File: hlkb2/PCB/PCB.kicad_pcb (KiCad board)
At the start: 2 copper layers, 228 x 76 mm, 101 parts, among them K1 KEYSW, K10 KEYSW, K11 KEYSW, K12 KEYSW, K13 KEYSW, K14 KEYSW, K15 KEYSW, K16 KEYSW, K17 KEYSW, K18 KEYSW, K19 KEYSW, K2 KEYSW, K20 KEYSW, K21 KEYSW, K22 KEYSW, K23 KEYSW, K24 KEYSW, K25 KEYSW, K26 KEYSW, K27 KEYSW, K28 KEYSW, K29 KEYSW, K3 KEYSW, K30 KEYSW, K31 KEYSW, K32 KEYSW, K33 KEYSW, K34 KEYSW, K35 KEYSW, K36 KEYSW, K37 KEYSW, K38 KEYSW, K39 KEYSW, K4 KEYSW, K40 KEYSW, K41 KEYSW, K42 KEYSW, K43 KEYSW, K44 KEYSW, K45 KEYSW, K46 KEYSW, K47 KEYSW, K48 KEYSW, K5 KEYSW, K6 KEYSW, K7 KEYSW, K8 KEYSW, K9 KEYSW

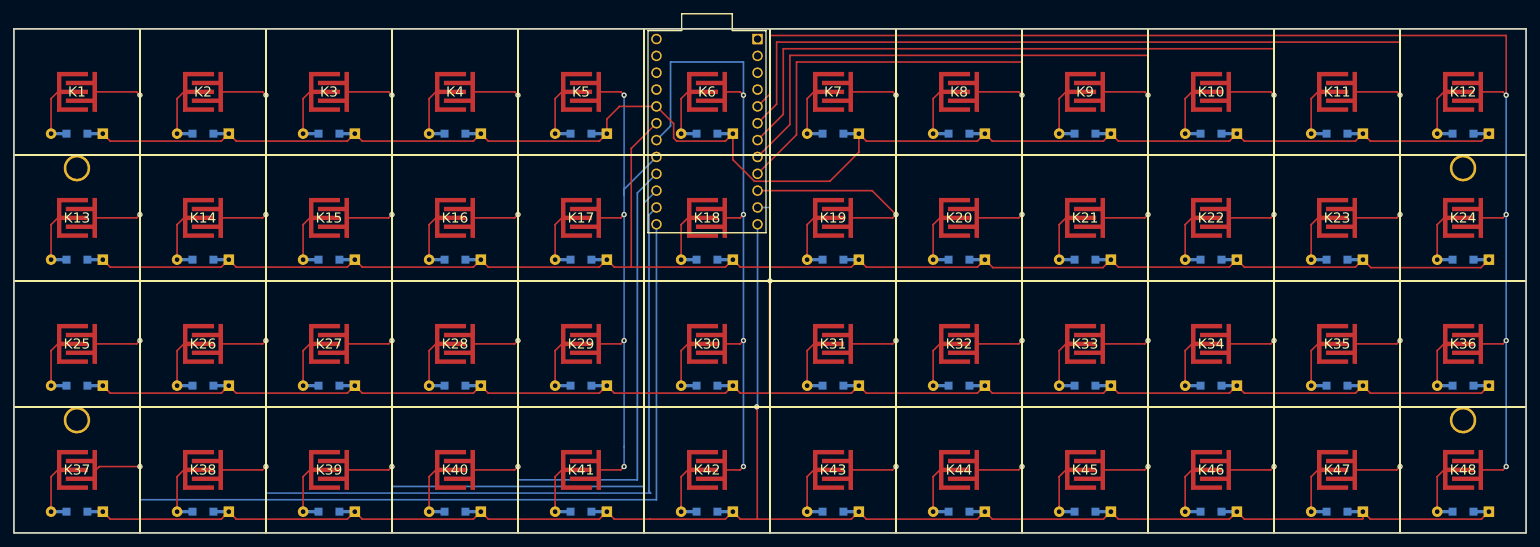
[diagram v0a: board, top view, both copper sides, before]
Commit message: Add 3mm contact pad, update PCB
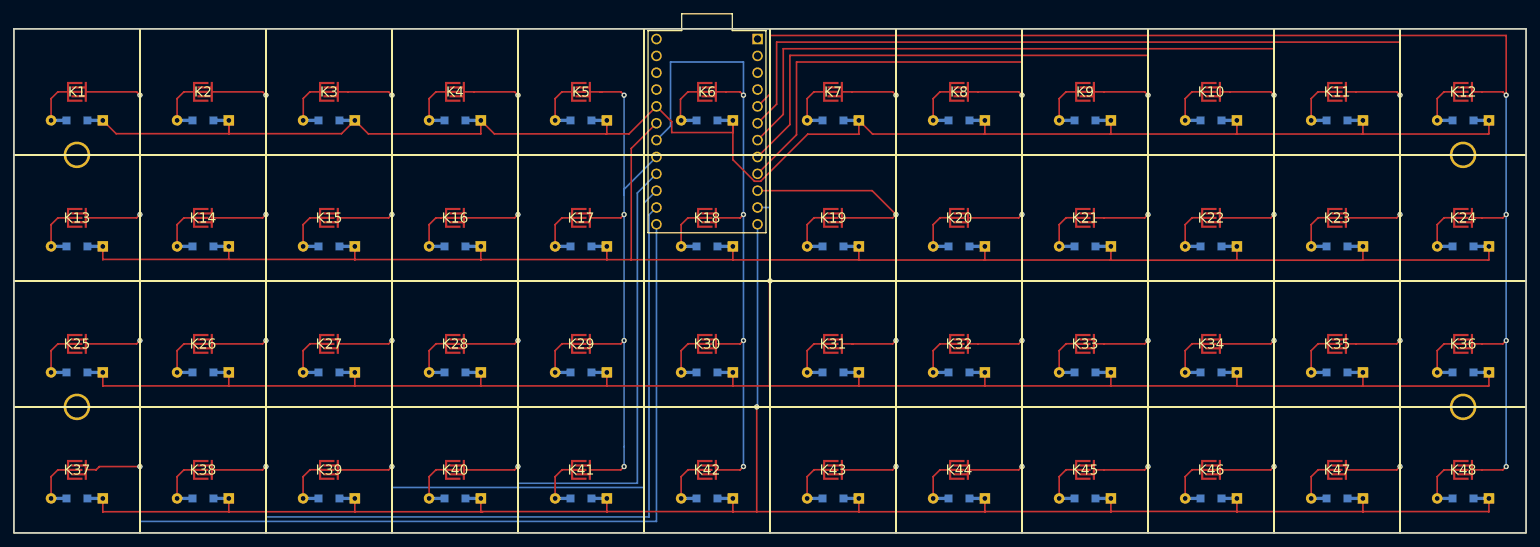
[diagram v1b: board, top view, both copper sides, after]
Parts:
- K1, K10, K11, K12, K13, K14, K15, K16, K17, K18, K19, K2, K20, K21, K22, K23, K24, K25, K26, K27, K28, K29, K3, K30, K31, K32, K33, K34, K35, K36, K37, K38, K39, K4, K40, K41, K42, K43, K44, K45, K46, K47, K48, K5, K6, K7, K8, K9: footprint contact_pad:contact_pad_6mm -> contact_pad:contact_pad_3mm
- moved D1 2.00 mm to (46.0, 75.2)
- moved D10 2.00 mm to (217.0, 75.2)
- moved D11 2.00 mm to (236.0, 75.2)
- moved D12 2.00 mm to (255.0, 75.2)
- moved D13 2.00 mm to (46.0, 94.2)
- moved D14 2.00 mm to (65.0, 94.2)
- moved D15 2.00 mm to (84.0, 94.2)
- moved D16 2.00 mm to (103.0, 94.2)
- moved D17 2.00 mm to (122.0, 94.2)
- moved D18 2.00 mm to (141.0, 94.2)
- moved D19 2.00 mm to (160.0, 94.2)
- moved D2 2.00 mm to (65.0, 75.2)
- moved D20 2.00 mm to (179.0, 94.2)
- moved D21 2.00 mm to (198.0, 94.2)
- moved D22 2.00 mm to (217.0, 94.2)
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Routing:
- net /row1: track 234.2 -> 250.0 mm
- net /row3: track 249.1 -> 262.2 mm
- net /col2: track 188.9 -> 201.9 mm
- net /row2: track 242.6 -> 255.5 mm
- net /col1: track 207.7 -> 220.4 mm
- net /row4: track 264.4 -> 276.6 mm
- net /col4: track 150.6 -> 157.8 mm
- net /col3: track 169.7 -> 176.1 mm
- net /col5: track 79.0 -> 85.3 mm
- net /col7: track 105.7 -> 111.9 mm
- net /col8: track 141.6 -> 147.7 mm
- net /col6: track 96.0 -> 102.0 mm
- net /col10: track 179.7 -> 185.8 mm
- net /col9: track 160.6 -> 166.7 mm
- net /col11: track 198.7 -> 204.8 mm
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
